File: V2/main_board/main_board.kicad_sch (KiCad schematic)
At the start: 85 parts, among them J1 Conn_02x14_Top_Bottom, J2 OUT_1, J3 OUT_2, J5 EXT_TEMP, J6 USB_C_Receptacle_USB2.0_16P, K1 Relay_SPST_Latching_2coil, K2 Relay_SPST_Latching_2coil, Q1 BC817, Q2 BC817, Q3 BC817, Q4 BC817, SW1 SW_Slide_DPDT, SW2 SW_Push, SW3 SW_Push, U1 BQ24074RGT, U10 ESP32-S3-WROOM-2, U11 LTV-217, U2 AP7361C-33E, U3 MAX17048G_T10, U4 LTV-217, U5 LTV-217, U6 PCF8563T, U7 LTV-217, U8 DS18B20Z, U9 DS18B20Z, Y1 32.768khz

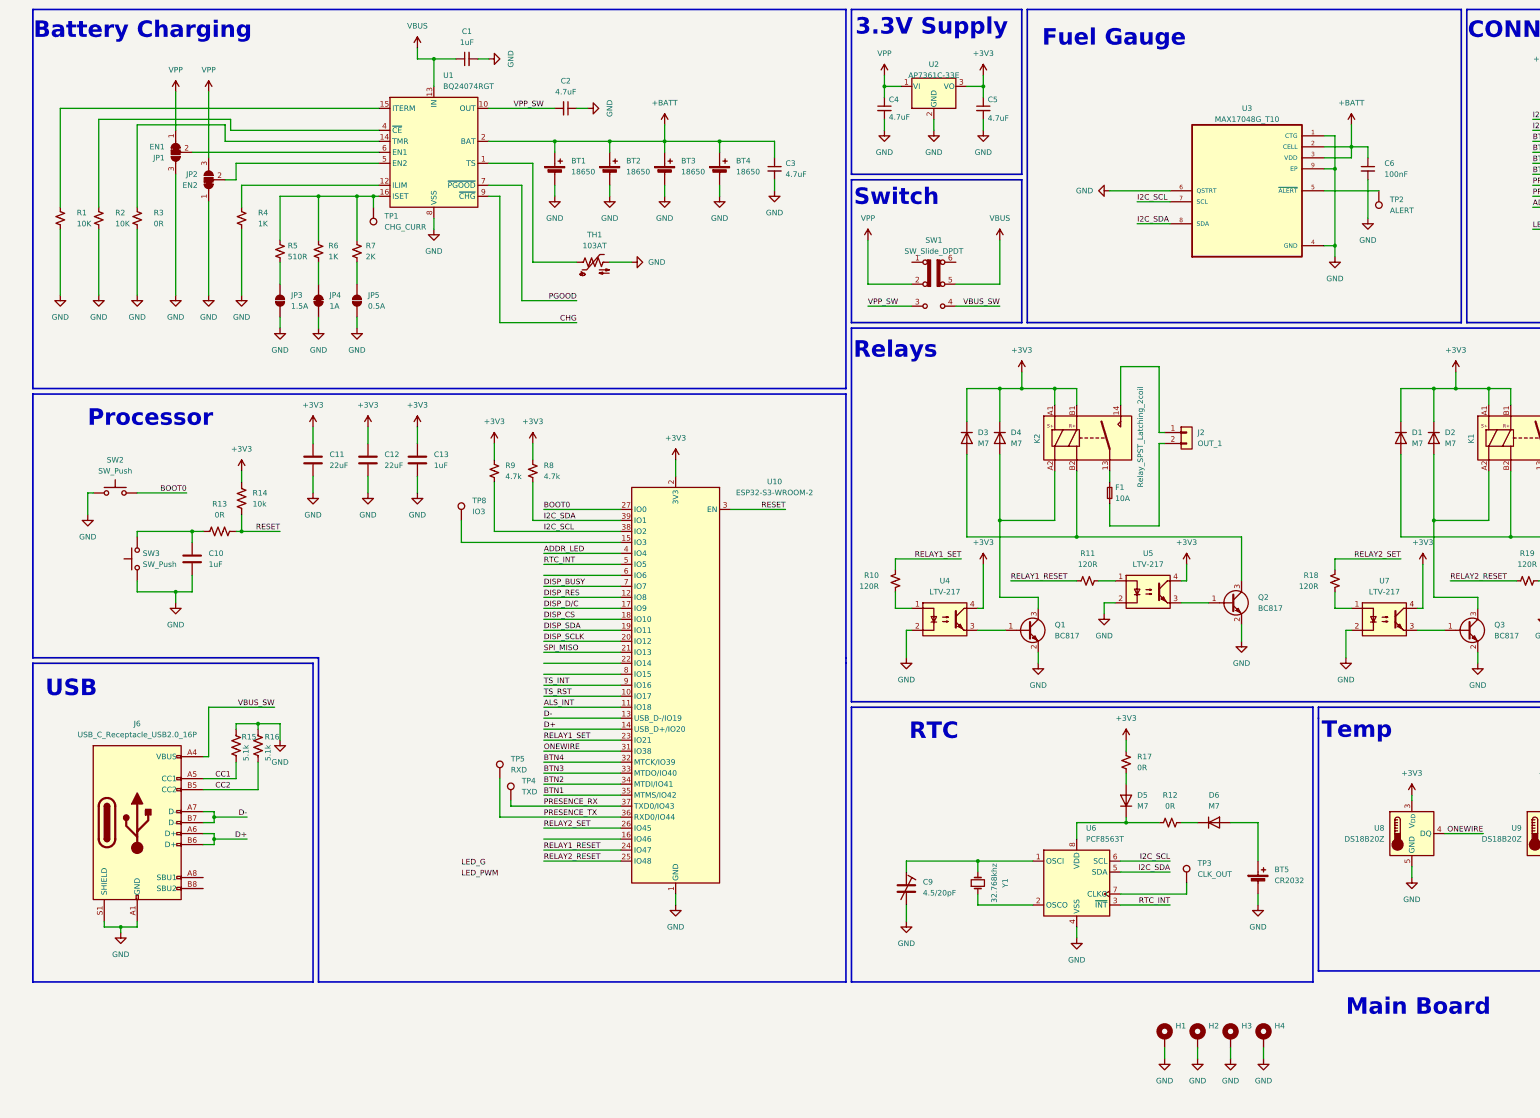
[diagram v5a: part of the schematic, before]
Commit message: Schematic updates
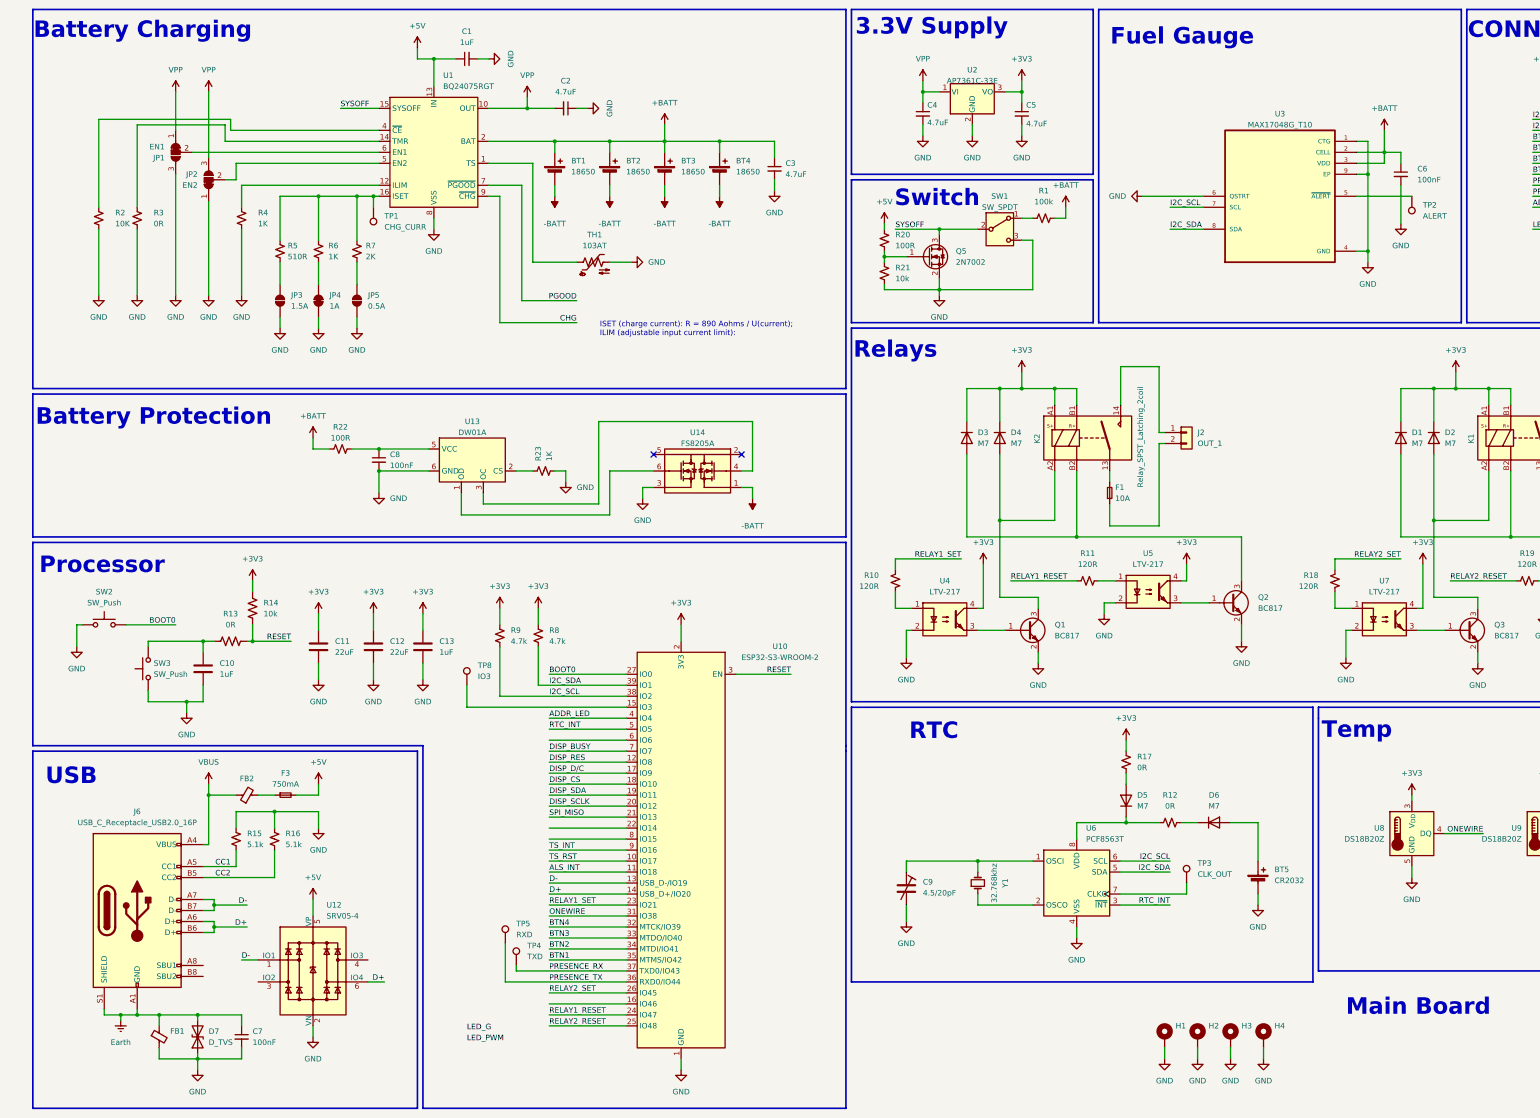
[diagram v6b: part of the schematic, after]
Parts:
- removed R1: 10K, Resistor_SMD:R_0603_1608Metric, symbol *partsbox:0603-10Kohm
- removed SW1: SW_Slide_DPDT, Button_Switch_THT:SW_E-Switch_EG2219_DPDT_Angled, symbol *partsbox:EG2219
- removed U1: BQ24074RGT, Package_DFN_QFN:VQFN-16-1EP_3x3mm_P0.5mm_EP1.6x1.6mm, symbol Battery_Management:BQ24074RGT
- added C7, C8: 100nF, Capacitor_SMD:C_0603_1608Metric, symbol *partsbox:0603-100nF
- added D7: D_TVS, Diode_SMD:D_SOD-323, symbol *partsbox:H8VHD3B
- added F3: 750mA, Fuse:Fuse_1206_3216Metric_Pad1.42x1.75mm_HandSolder, symbol Device:Fuse_Small
- added FB1, FB2: FerriteBead_Small, Inductor_SMD:L_0603_1608Metric, symbol *partsbox:BLM18PG121SN1D
- added Q5: 2N7002, Package_TO_SOT_SMD:SOT-23, symbol *partsbox:2N7002
- added R1: 100k, Resistor_SMD:R_0603_1608Metric, symbol *partsbox:0603-100Kohm
- added R20, R22: 100R, Resistor_SMD:R_0603_1608Metric, symbol *partsbox:0603-100ohm
- added R21: 10k, Resistor_SMD:R_0603_1608Metric, symbol *partsbox:0603-10Kohm
- added R23: 1K, Resistor_SMD:R_0603_1608Metric, symbol *partsbox:0603-1Kohm
- added SW1: SW_SPDT, Button_Switch_THT:SW_E-Switch_EG1224_SPDT_Angled, symbol *partsbox:EG1224
- added U1: BQ24075RGT, Package_DFN_QFN:VQFN-16-1EP_3x3mm_P0.5mm_EP1.6x1.6mm, symbol *partsbox:BQ24075TRGTR
- added U12: SRV05-4, Package_TO_SOT_SMD:SOT-23-6, symbol *partsbox:SRV05-4-P-T7
- added U13: DW01A, Package_TO_SOT_SMD:SOT-23-6, symbol *partsbox:DW01A
- added U14: FS8205A, Package_TO_SOT_SMD:SOT-23-6, symbol *partsbox:FS8205A
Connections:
- net VBUS_SW is gone; now on net VBUS: J6.A4 (VBUS), J6.A9 (VBUS), J6.B4 (VBUS), J6.B9 (VBUS)
- net VPP_SW is gone; now on net VPP: C2.2
- net +BATT: now also R1.2, R22.1, U1.2 (BAT), U1.3 (BAT)
- net CHG: now also U1.9 (~{CHG})
- net D+: now also U12.6 (IO4)
- net D-: now also U12.1 (IO1)
- net GND: now also C7.2, C8.2, D7.1 (A1), FB1.2, Q5.2 (S), R21.2, R23.2, SW1.3 (C), U1.17 (VSS), U1.8 (VSS), U12.2 (VN), U13.6 (GND), U14.3 (S2); no longer BT1.2 (-), BT2.2 (-), BT3.2 (-), BT4.2 (-), J6.A1 (GND), J6.A12 (GND), J6.B1 (GND), J6.B12 (GND), J6.S1 (SHIELD)
- net PGOOD: now also U1.7 (~{PGOOD})
- net VBUS: now also FB2.1; no longer C1.1
- net VPP: now also U1.10 (OUT), U1.11 (OUT)
- net at R3.1: now also U1.14 (TMR)
- net at R4.1: now also U1.12 (ILIM)
- net at TH1.1: now also U1.1 (TS)
- net at JP1.2 (C): now also U1.6 (EN1)
- net at R5.1, R6.1, R7.1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: now also U1.16 (ISET)
- net at JP2.2 (C): now also U1.5 (EN2)
- net at R2.1: now also U1.4 (~{CE})
- new net: Q5.1 (G), R20.2, R21.1
- new net: C8.1, R22.2, U13.5 (VCC)
- new net: F3.1, FB2.2
- new net: U13.1 (OD), U14.6 (G2)
- new net: R23.1, U13.2 (CS)
- new net: U13.3 (OC), U14.4 (G1)
- new net: R1.1, SW1.1 (A)
- new net +5V: C1.1, F3.2, R20.1, U1.13 (IN), U12.5 (VP)
- new net -BATT: BT1.2 (-), BT2.2 (-), BT3.2 (-), BT4.2 (-), U14.1 (S1)
- new net Earth: C7.1, D7.2 (A2), FB1.1, J6.A1 (GND), J6.A12 (GND), J6.B1 (GND), J6.B12 (GND), J6.S1 (SHIELD)
- new net SYSOFF: Q5.3 (D), SW1.2 (B), U1.15 (SYSOFF)
- no-connect marks 0 -> 2
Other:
- note added: "Battery Protection"
- note added: "ISET (charge current): R = 890 Aohms / U(current); ILIM (adjustable input current limit):"
- moved on the sheet: C10, C11, C12, C13, C4, C5, C6, J6, R13, R14, R8, R9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

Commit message: main board in good spot
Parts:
- removed JP3: 1.5A, Jumper:SolderJumper-2_P1.3mm_Open_RoundedPad1.0x1.5mm, symbol Jumper:SolderJumper_2_Open
- removed R2: 10K, Resistor_SMD:R_0603_1608Metric, symbol *partsbox:0603-10Kohm
- removed R5: 510R, Resistor_SMD:R_0603_1608Metric, symbol *partsbox:0603-510ohm
- removed R6: 1K, Resistor_SMD:R_0603_1608Metric, symbol *partsbox:0603-1Kohm
- removed R7: 2K, Resistor_SMD:R_0603_1608Metric, symbol *partsbox:0603-2Kohm
- added R1: 47k, Resistor_SMD:R_0603_1608Metric, symbol *partsbox:0603-47Kohm
- added R8: 3.9k, Resistor_SMD:R_0603_1608Metric, symbol *partsbox:0603-3.9Kohm
- added R9: 910R, Resistor_SMD:R_0603_1608Metric, symbol *partsbox:0603-910ohm
- added TP2, TP3, TP5: IO3, TestPoint:TestPoint_Pad_2.0x2.0mm, symbol Connector:TestPoint
- F1: renamed from F3; value 750mA -> 2A
- JP3: renamed from JP4; value 1A -> 230mA
- JP4: renamed from JP5; value 0.5A -> 930mA
- R5: renamed from R4; now not fitted; now left out of the parts list
- renumbered C10 to C1, C9 to C10, C4 to C11, C5 to C12, C6 to C13, C7 to C2, C11 to C3, C12 to C4, C8 to C5, C13 to C6, C1 to C7, C2 to C8, C3 to C9, D7 to D1, D3 to D2, D4 to D3, D5 to D4, D6 to D5, D1 to D6, D2 to D7, F1 to F2, F2 to F3, J6 to J1, J1 to J3, J3 to J4, K2 to K1, K1 to K2, Q5 to Q1, Q1 to Q2, Q2 to Q3, Q3 to Q4, Q4 to Q5, R22 to R10, R9 to R11, R8 to R12, R23 to R13, R20 to R14, R21 to R15, R10 to R16, R1 to R17, R11 to R18, R17 to R19, R3 to R2, R12 to R20, R18 to R21, R19 to R22, R13 to R3, R15 to R4, R14 to R6, R16 to R7, SW2 to SW1, SW3 to SW2, SW1 to SW3, TP8 to TP4, TP5 to TP6, TP4 to TP7, TP3 to TP8, TP2 to TP9, U12 to U1, U3 to U10, U7 to U11, U8 to U12, U9 to U13, U11 to U14, U1 to U2, U13 to U3, U10 to U4, U14 to U5, U4 to U6, U2 to U7, U6 to U8, U5 to U9
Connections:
- net SPI_MISO is gone; now on net LED_PWM: U4.21 (IO13)
- net ADDR_LED: now also U4.22 (IO14); no longer U4.4 (IO4)
- net ALS_INT: now also J3.20 (Pin_20), U4.8 (IO15); no longer U4.11 (IO18)
- net DISP_BUSY: now also U4.12 (IO8); no longer U4.7 (IO7)
- net DISP_RES: now also U4.11 (IO18); no longer U4.12 (IO8)
- net GND: now also R1.2; no longer J3.22 (Pin_22)
- net LED_G: now also J3.22 (Pin_22), U4.7 (IO7)
- net TS_INT: now also U4.10 (IO17); no longer U4.9 (IO16)
- net TS_RST: now also U4.9 (IO16); no longer U4.10 (IO17)
- net at JP4.2 (B): now also R9.2
- net at JP3.2 (B): now also R8.2
- net at TP1.1, U2.16 (ISET): now also R8.1, R9.1
- net at U2.4 (~{CE}): now also R1.1
- net at U4.16 (IO46): now also TP5.1
- net at U4.6 (IO6): now also TP2.1
- new net: TP3.1, U4.4 (IO4)
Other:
- note added: "ISET (charge current): 3.9kohm->230mA; 910ohm->980mA TMR: (10 x 48s/kOhm) * 47kOhm = 22560s = 6.27h"
- note removed: "ISET (charge current): R = 890 Aohms / U(current); ILIM (adjustable input current limit):"
- moved on the sheet: JP3, JP4, TP1, TP4

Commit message: Display board in good spot
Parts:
- added C14, C15: 100nF, Capacitor_SMD:C_0603_1608Metric, symbol *partsbox:0603-100nF
- J3: footprint Connector_PinHeader_2.54mm:PinHeader_2x14_P2.54mm_Vertical_SMD -> Connector_PinSocket_2.54mm:PinSocket_2x14_P2.54mm_Vertical_SMD
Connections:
- net +3V3: now also C14.1, C15.1
- net GND: now also C14.2, C15.2
